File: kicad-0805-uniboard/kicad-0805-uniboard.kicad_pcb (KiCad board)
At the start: 2 copper layers, 100 x 110 mm, 145 parts, among them J1 ICSP Header, J103 BA56_3DIG_7SEG, J104 Gate Out, J105 Clock Out, J106 Clock In, J107 Pitch Out, J108 CV Out, J109 Reset In, J4 RED_STRIPE, Q1 2N7002, Q101 MMBT3906, Q102 MMBT3906, Q103 MMBT3906, Q104 MMBT3904, Q105 MMBT3904, Q2 2N7002, Q3 2N7002, Q4 2N7002, SW101 Shift, SW102 Play, SW103 Load, SW104 Save, SW105 Repeat, SW106 Mutate, SW107 Glide, SW108 SW_Push, SW109 SW_Push, SW110 SW_Push, SW111 SW_Push, SW112 SW_Push, SW113 SW_Push, SW114 SW_Push, SW115 SW_Push, SW116 Rotary_Encoder, SW117 SW_Push, SW118 SW_Push, SW119 SW_Push, SW120 SW_Push, SW121 SW_Push, SW122 SW_Push, SW123 SW_Push, SW124 SW_Push, U1 AMS1117-5.0, U101 74HC595, U102 MCP23S17, U103 74HC595, U2 AMS1117-3.3, U3 ATMega328P, U4 W25Q80DVSN, U5 TL072, U6 MCP4822, Y1 16MHz

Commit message: Getting there.
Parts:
- C107, R108, R109, R110: moved to B.Cu
- moved R112 36.8 mm to (140.5, 62.2), turned to 270 degrees
- moved R113 33.3 mm to (143.9, 62.2), turned to 270 degrees
- moved C108 29.5 mm to (140.9, 46.4), turned to 180 degrees
- moved C109 29.2 mm to (140.9, 44.4), turned to 180 degrees
- moved R108 25.5 mm to (151.9, 62.2), turned to 270 degrees
- moved R109 21.9 mm to (149.2, 62.2), turned to 270 degrees
- moved J1 20.9 mm to (134.2, 54.0), turned to 180 degrees
- moved U103 20.0 mm to (147.8, 49.8)
- moved R110 18.7 mm to (146.8, 62.2), turned to 270 degrees
- moved C107 12.6 mm to (140.6, 52.9), turned to 270 degrees
- moved R111 11.7 mm to (134.7, 49.4)
- moved R2 10.2 mm to (132.7, 62.1), turned to 180 degrees
- moved R107 6.11 mm to (134.7, 46.9)
- moved R106 6.02 mm to (134.7, 44.5)
- moved C5 2.45 mm to (121.4, 64.2), turned to 0 degrees
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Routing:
- net Net-(J103-Pad1): track 0.00 -> 75.1 mm
- net Net-(J103-Pad2): track 0.00 -> 72.7 mm, vias 0 -> 2
- net Net-(J103-Pad4): track 0.00 -> 69.6 mm, vias 0 -> 2
- net Net-(J103-Pad3): track 0.00 -> 64.8 mm
- net Net-(J103-Pad5): track 0.00 -> 56.3 mm
- net AD2: track 0.00 -> 55.9 mm, vias 0 -> 1
- net MISO: track 27.7 -> 74.5 mm, vias 2 -> 4
- net CS3: track 7.44 -> 39.5 mm, vias 0 -> 1
- net AD1: track 0.00 -> 29.4 mm, vias 0 -> 1
- net Net-(U101-Pad9): track 0.00 -> 26.2 mm
- net +5V: track 478.5 -> 500.2 mm
- net Net-(R106-Pad1): track 0.57 -> 22.2 mm, vias 0 -> 1
- net CS0: track 4.52 -> 25.5 mm
- net MOSI: track 57.2 -> 77.8 mm, vias 4 -> 5
- net SCK: track 67.1 -> 87.0 mm
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
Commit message: More dots connected.
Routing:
- net +5V: track 500.2 -> 536.1 mm, vias 4 -> 5
- net Net-(R109-Pad1): track 0.00 -> 19.7 mm
- net Net-(R110-Pad1): track 0.00 -> 18.9 mm
- net Net-(R108-Pad1): track 0.00 -> 18.7 mm
- net Net-(R112-Pad1): track 0.00 -> 16.4 mm
- net Net-(R113-Pad1): track 0.00 -> 16.2 mm
- net MOSI: track 77.8 -> 88.8 mm
- net RESET: track 3.22 -> 12.1 mm
- net Net-(R111-Pad1): track 14.5 -> 20.5 mm, vias 0 -> 1
- net GND: vias 33 -> 36

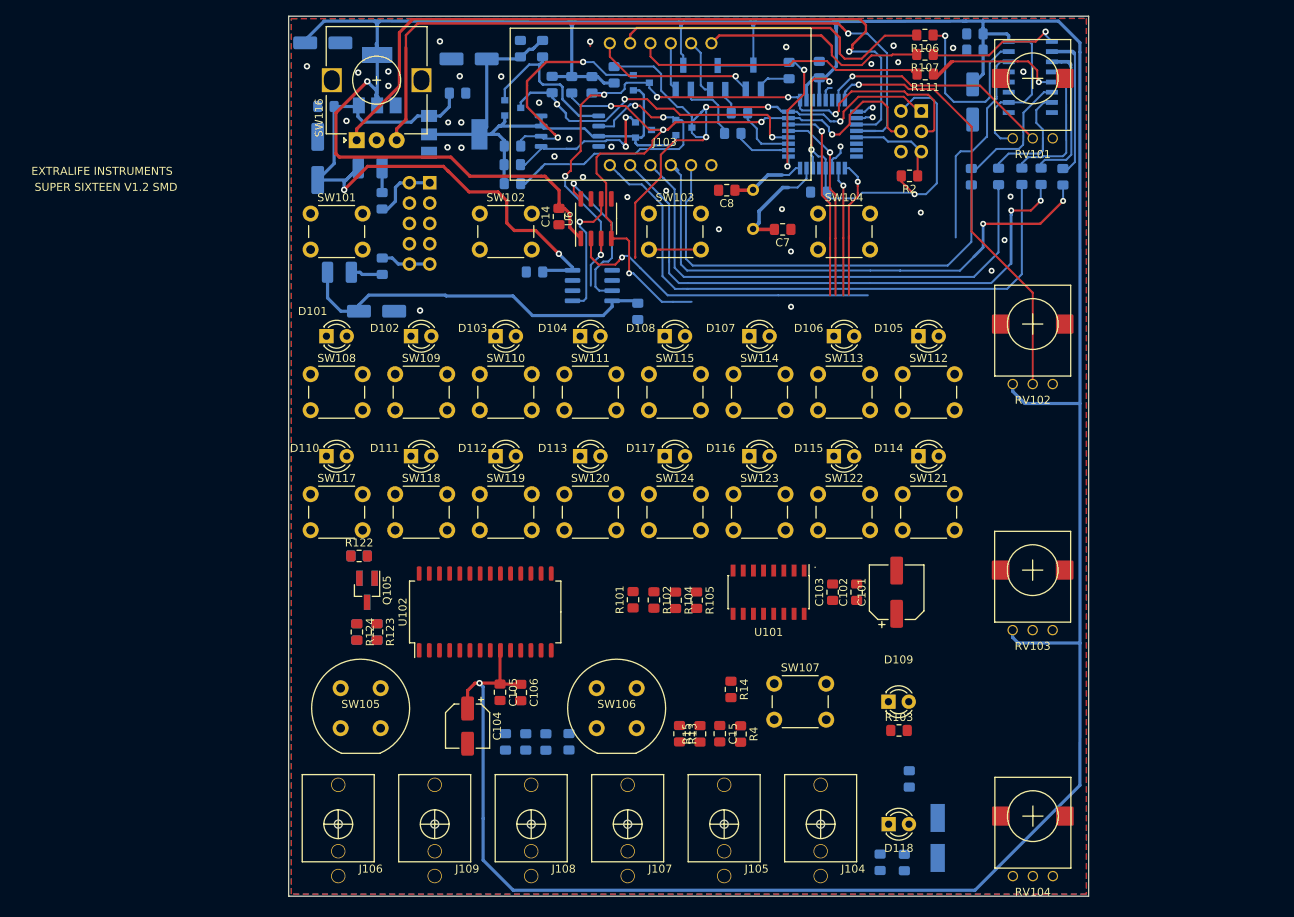
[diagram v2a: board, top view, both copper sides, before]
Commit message: More routing added. The top third of the board is filled in.
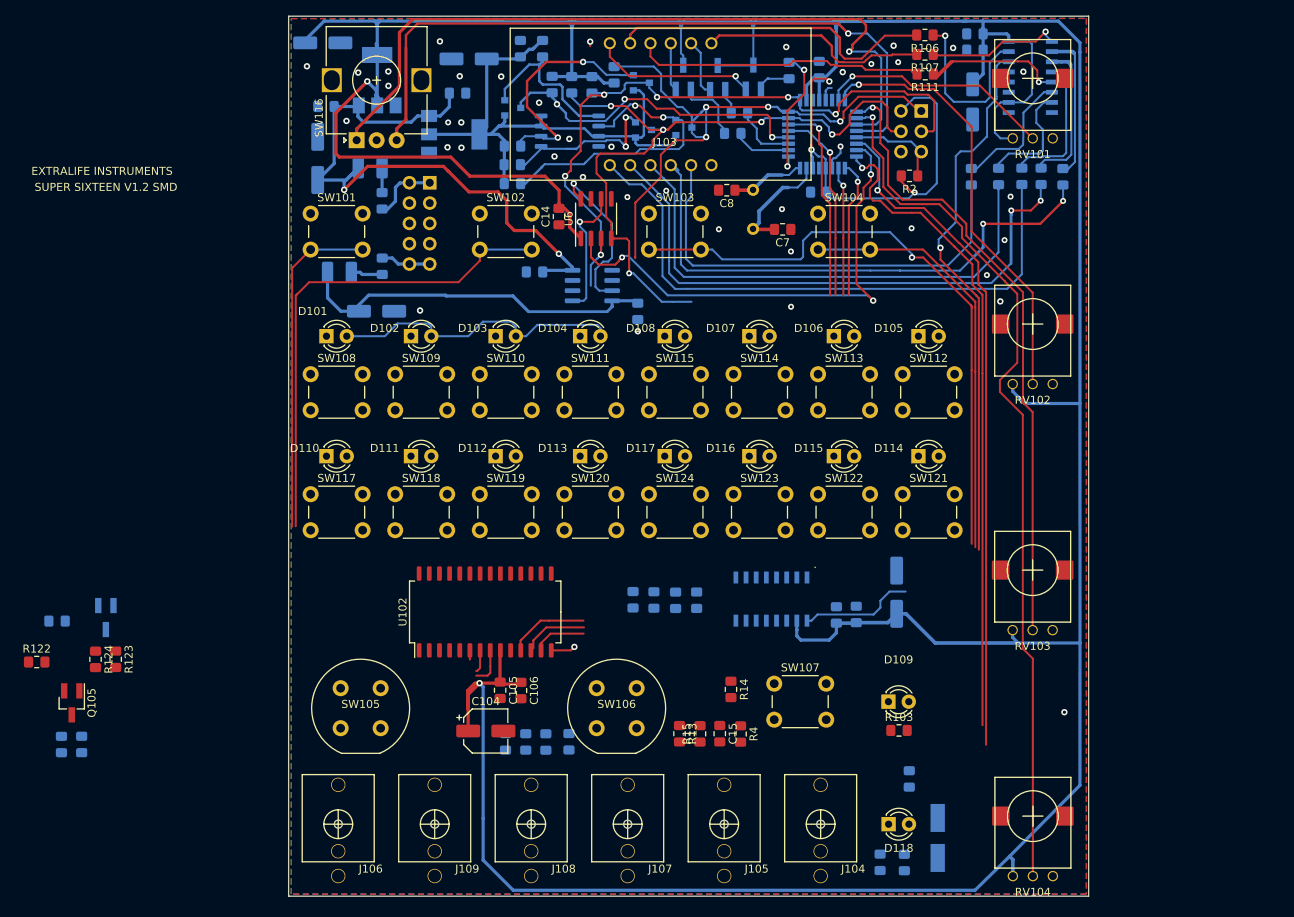
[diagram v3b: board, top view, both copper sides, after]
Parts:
- C101, C102, C103, R101, R102, R104, R105, U101: moved to B.Cu
- moved R122 42.4 mm to (23.6, 122.9)
- moved R121 39.5 mm to (26.7, 133.2)
- moved Q105 39.5 mm to (28.0, 128.0)
- moved R120 39.5 mm to (29.2, 133.2)
- moved R119 38.6 mm to (26.2, 117.8)
- moved R123 32.8 mm to (33.5, 122.5)
- moved R124 32.8 mm to (31.0, 122.6)
- moved Q104 32.8 mm to (32.3, 117.3)
- moved C103 2.88 mm to (123.6, 117.0)
- moved C102 2.78 mm to (126.1, 116.9)
- moved C104 2.35 mm to (79.8, 131.5), turned to 0 degrees
- moved U101 0.93 mm to (115.5, 115.0)
- moved C105 0.25 mm to (81.6, 126.4)
- moved C106 0.25 mm to (84.2, 126.5)
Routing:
- net AD4: track 2.06 -> 109.9 mm
- net Net-(R3-Pad1): track 0.00 -> 84.9 mm, vias 0 -> 1
- net Net-(R4-Pad1): track 0.00 -> 82.4 mm, vias 0 -> 1
- net AD3: track 2.25 -> 79.1 mm
- net /A2: track 6.50 -> 77.4 mm, vias 0 -> 1
- net /A1: track 0.00 -> 61.6 mm
- net Net-(U101-Pad9): track 26.2 -> 82.5 mm, vias 0 -> 1
- net /A3: track 0.00 -> 53.0 mm
- net +5V: track 536.1 -> 581.8 mm
- net /A0: track 0.00 -> 42.1 mm
- net Net-(D101-Pad2): track 0.00 -> 37.7 mm
- net CS3: track 39.5 -> 62.2 mm, vias 1 -> 3
- net CS0: track 25.5 -> 35.6 mm
- net SCK: track 87.0 -> 95.4 mm
- net MOSI: track 88.8 -> 95.6 mm
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
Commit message: More routes added.
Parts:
- moved C4 1.36 mm to (98.0, 80.2)
- moved U101 0.97 mm to (116.2, 115.7), turned to 0 degrees
- moved R2 0.62 mm to (133.1, 61.6)
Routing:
- net Net-(SW108-Pad2): track 0.00 -> 138.5 mm, vias 0 -> 1
- net Net-(SW109-Pad2): track 0.00 -> 119.4 mm
- net Net-(D101-Pad1): track 0.00 -> 108.1 mm
- net Net-(SW112-Pad1): track 0.00 -> 96.3 mm, vias 0 -> 1
- net Net-(D102-Pad1): track 0.00 -> 87.3 mm
- net Net-(SW121-Pad1): track 0.00 -> 70.7 mm, vias 0 -> 1
- net Net-(SW108-Pad1): track 0.00 -> 66.3 mm
- net Net-(D103-Pad1): track 0.00 -> 64.9 mm
- net MOSI: track 95.6 -> 160.3 mm, vias 5 -> 6
- net Net-(C16-Pad1): track 0.00 -> 64.1 mm, vias 0 -> 1
- net Net-(C16-Pad2): track 0.00 -> 59.3 mm, vias 0 -> 1
- net Net-(D105-Pad2): track 0.00 -> 58.2 mm
- net Net-(SW111-Pad2): track 0.00 -> 54.7 mm, vias 0 -> 1
- net Net-(SW117-Pad1): track 0.00 -> 49.1 mm
- net Net-(D104-Pad1): track 0.00 -> 43.6 mm
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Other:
- board text removed: "."

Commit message: Initial routing complete.
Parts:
- R103, R123, R124, R4: moved to B.Cu
- R119: moved to F.Cu
- moved Q105 52.0 mm to (79.1, 137.3), turned to 0 degrees
- moved R122 51.0 mm to (73.7, 132.5), turned to 270 degrees
- moved R119 47.6 mm to (71.4, 132.5), turned to 270 degrees
- moved R124 40.4 mm to (68.6, 137.2)
- moved R123 40.1 mm to (70.8, 137.2)
- moved R121 39.8 mm to (66.3, 137.2)
- moved R120 35.0 mm to (64.0, 137.2)
- moved Q104 31.1 mm to (58.2, 134.6), turned to 90 degrees
- moved R118 10.7 mm to (130.0, 137.5), turned to 270 degrees
- moved R4 9.51 mm to (120.4, 135.4), turned to 180 degrees
- moved R104 6.24 mm to (97.2, 115.0)
- moved R17 6.17 mm to (92.5, 138.6)
- moved R18 6.17 mm to (89.6, 138.6)
- moved R15 3.41 mm to (110.0, 131.9), turned to 270 degrees
- moved C16 3.31 mm to (88.0, 133.5)
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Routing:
- net ClockIn: track 22.7 -> 194.7 mm, vias 1 -> 6
- net /A2: track 77.4 -> 229.6 mm, vias 1 -> 3
- net ResetIn: track 21.7 -> 172.6 mm, vias 1 -> 3
- net /A3: track 53.0 -> 192.4 mm, vias 0 -> 2
- net CS0: track 43.1 -> 180.8 mm, vias 1 -> 3
- net MOSI: track 160.3 -> 267.0 mm, vias 6 -> 7
- net Net-(C16-Pad2): track 59.3 -> 140.7 mm, vias 1 -> 4
- net Net-(C15-Pad1): track 0.00 -> 77.0 mm, vias 0 -> 1
- net Net-(C15-Pad2): track 0.00 -> 73.9 mm, vias 0 -> 1
- net Net-(C16-Pad1): track 64.1 -> 136.8 mm, vias 1 -> 4
- net /A7: track 4.73 -> 68.7 mm, vias 0 -> 1
- net /A6: track 2.86 -> 65.3 mm, vias 0 -> 1
- net SCK: track 126.7 -> 188.7 mm, vias 7 -> 11
- net MISO: track 77.5 -> 136.4 mm, vias 5 -> 7
- net CS1: track 30.9 -> 71.1 mm, vias 1 -> 2
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
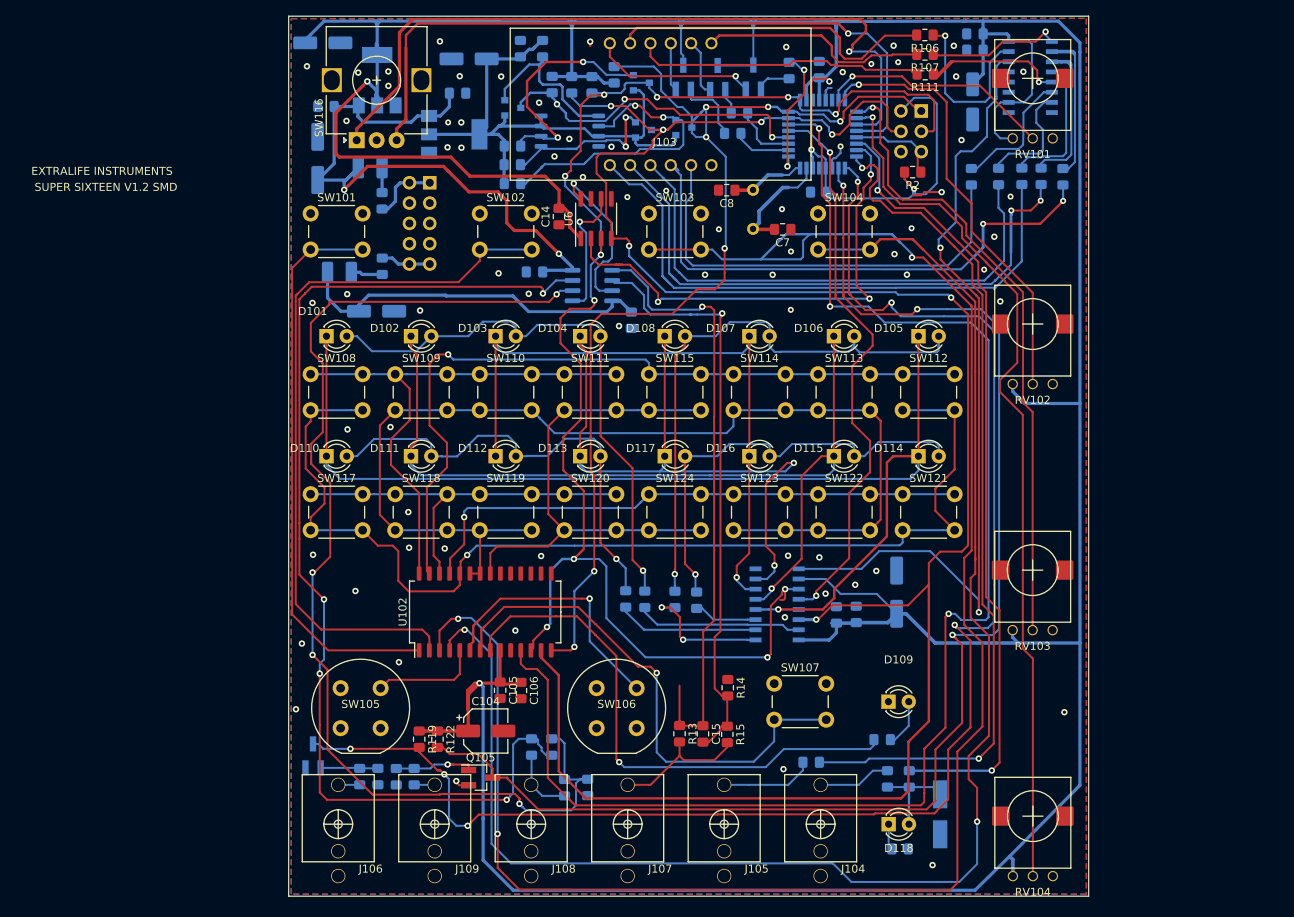
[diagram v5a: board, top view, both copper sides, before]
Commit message: Improved ground planes.
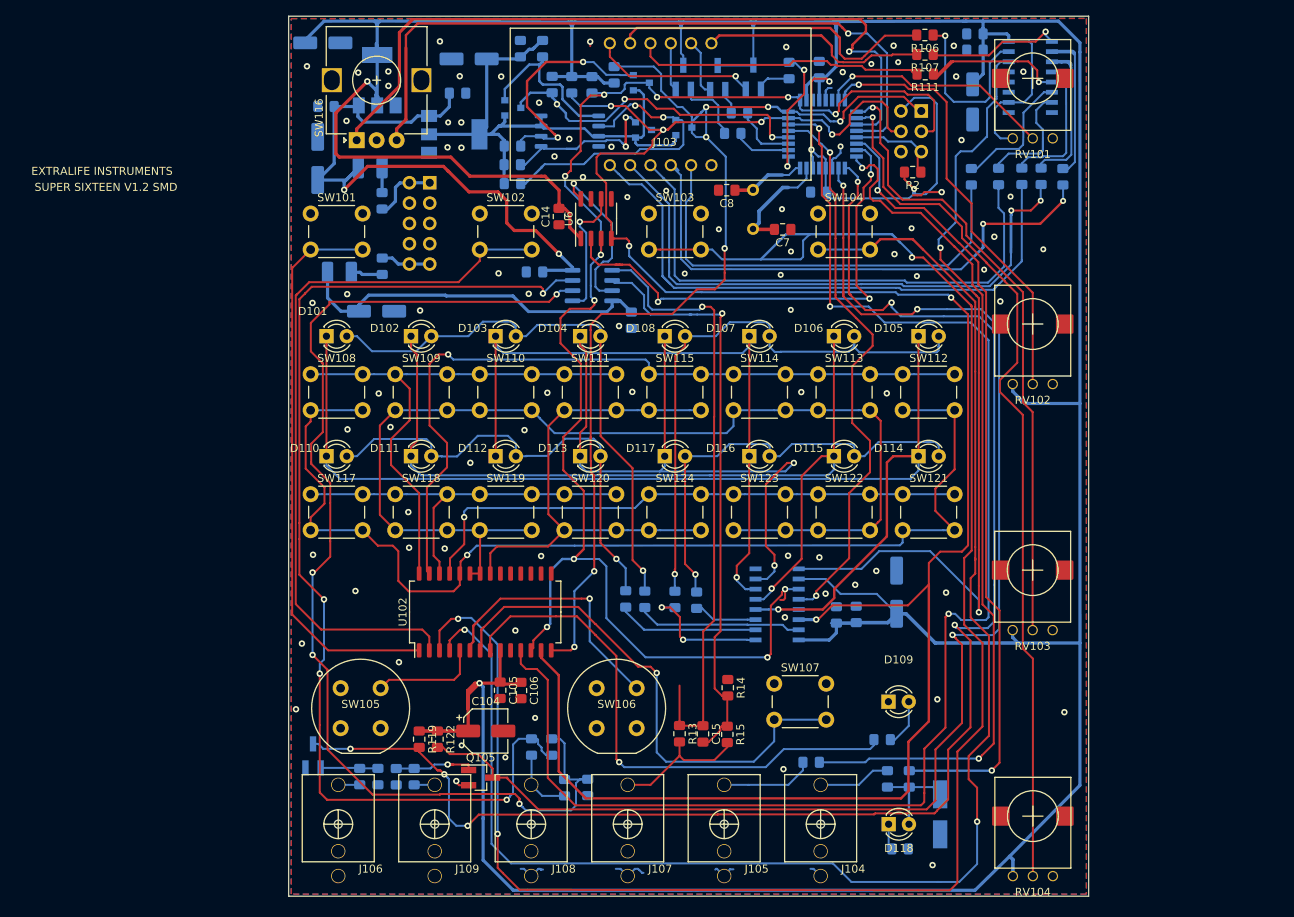
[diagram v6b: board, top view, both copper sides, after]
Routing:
- net GND: track 11.6 -> 24.3 mm, vias 71 -> 84
- net Net-(J103-Pad3): track 66.8 -> 68.0 mm
